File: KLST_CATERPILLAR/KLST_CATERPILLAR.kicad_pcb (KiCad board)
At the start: 6 copper layers, 148.5 x 105 mm, 242 parts, among them J1 Micro_SD_Card_Det_Hirose_DM3AT, J10 HOST(DFP), J11 DAC, J12 ADC, J13 GPIO, J14 ARM_JTAG_SWD(STDC14), J15 TC2070-IDC-NL, J16 MIC_IN, J17 LINE_IN, J18 HEADPHONE_OUT+MIC, J19 LINE_OUT, J2 FPC-40, J3 Battery_18650_Plus, J4 Battery_18650_Minus, J5 UART, J6 UART, J7 MIDI_IN, J8 MIDI_OUT, J9 DEVICE+CHARGE(UFP), Q1 AO3401A, Q2 BCM857BS, Q3 AO3401A, Q4 AO3401A, SW1 BUTTON_RESET, SW2 BUTTON_BOOT_FLASH, SW3 SW_SPDT, SW4 ENCODER, SW5 ENCODER, SW6 BUTTON, SW7 BUTTON, SW8 BUTTON, U1 AMS1117-3.3, U10 MP34DT05TR-A, U11 MP34DT05TR-A, U12 S70KL1282, U13 WM8904CGEFL/V, U14 AMS1117-1.8, U2 STM32H723ZGTx, U3 CAT4139TD-GT3, U4 TP5400, U5 H11L1SR2M, U6 74AHC1G125, U7 ECMF02-2AMX6, U8 TPS2041B, U9 TLV9001IDCK, Y1 16MHz

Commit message: reduced modules
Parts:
- removed C31: 1uF, Capacitor_SMD:C_0805_2012Metric
- removed C32: 4.7uF, Capacitor_SMD:C_0805_2012Metric
- removed C33, C35: 100nF, Capacitor_SMD:C_0805_2012Metric
- removed C34, C36: 22uF, Capacitor_SMD:C_0805_2012Metric
- removed C37: 47uF, Capacitor_SMD:CP_Elec_4x5.4
- removed C38, C39, C40, C41, C42, C43, C44, C45, C52, C53, C54, C55, C56: 100nF, Capacitor_SMD:C_0402_1005Metric
- removed D10, D14, D4: SS14, Diode_SMD:D_SMA
- removed D11: 1N914WT, Diode_SMD:D_SOD-523
- removed D5: LED_STDBY, LED_SMD:LED_0805_2012Metric
- removed D6: LED_CHRG, LED_SMD:LED_0805_2012Metric
- removed D7: SS32, Diode_SMD:D_SMA
- removed H1, H2, H3, H4: M3 Mounting Hole, MountingHole:MountingHole_3.2mm_M3_Pad_Via
- removed J11: DAC, PJ-316A-6A:PJ-316A-6A
- removed J12: ADC, PJ-316A-6A:PJ-316A-6A
- removed J2: FPC-40, THD0525-40CL-GF:CONN-SMD_40P-P0.50-H_THD0525-40CL-GF
- removed J3: Battery_18650_Plus, MY-18650-01:MY-18650-01
- removed J4: Battery_18650_Minus, MY-18650-01:MY-18650-01
- removed J6: UART, Connector_IDC:IDC-Header_2x03_P2.54mm_Horizontal
- removed J7: MIDI_IN, PJ-316A-6A:PJ-316A-6A
- removed J8: MIDI_OUT, PJ-316A-6A:PJ-316A-6A
- removed L2: 22uH, Inductor_SMD:L_Changjiang_FNR4030S
- removed L3: 10uH, Inductor_SMD:L_Changjiang_FNR4030S
- removed Q2: BCM857BS, Package_TO_SOT_SMD:SOT-363_SC-70-6
- removed Q3: AO3401A, Package_TO_SOT_SMD:SOT-23
- removed R18: 20R, Resistor_SMD:R_0805_2012Metric_Pad1.20x1.40mm_HandSolder
- removed R19: 1K, Resistor_SMD:R_1210_3225Metric
- removed R20, R21: 2K, Resistor_SMD:R_0805_2012Metric_Pad1.20x1.40mm_HandSolder
- removed R22: 1.2K, Resistor_SMD:R_0805_2012Metric_Pad1.20x1.40mm_HandSolder
- removed R23: 10K, Resistor_SMD:R_1210_3225Metric
- removed R24: 47K, Resistor_SMD:R_1210_3225Metric
- removed R25, R26, R27, R29, R30, R31, R32, R33, R35, R36, R37, R50, R52, R63: 10K, Resistor_SMD:R_0402_1005Metric
- removed R28, R34, R38, R51, R53: 1K, Resistor_SMD:R_0402_1005Metric
- removed R39: 220R, Resistor_SMD:R_0805_2012Metric
- removed R40, R41: 47R, Resistor_SMD:R_0805_2012Metric
- removed R42: 470R, Resistor_SMD:R_0805_2012Metric
- removed R47: 100K, Resistor_SMD:R_0805_2012Metric
- removed R48, R49: 20K, Resistor_SMD:R_0805_2012Metric
- removed R5, R6: 2.2K, Resistor_SMD:R_0402_1005Metric
- removed R60, R61, R62, R64, R65, R66, R67, R68, R69, R70, R71: 33R, Resistor_SMD:R_0402_1005Metric
- removed SW3: SW_SPDT, MK-12F03-G015:MK-12F03-G015
- removed SW4, SW5: ENCODER, PEC11R-4015F-S0024:PEC11R-4015F-S0024
- removed SW6: BUTTON, Button_Switch_SMD:SW_Push_SPST_NO_Alps_SKRK
- removed SW7, SW8: BUTTON, Cherry_MX:SW_Cherry_MX_PCB
- removed U12: S70KL1282, S70KL1282:BGA24C100P5X5_600X800X100
- removed U3: CAT4139TD-GT3, CAT4139TD-GT3:SOT95P280X100-5N
- removed U4: TP5400, Package_SO:SOP-8_3.9x4.9mm_P1.27mm
- removed U5: H11L1SR2M, Package_DIP:SMDIP-6_W9.53mm
- removed U6: 74AHC1G125, Package_TO_SOT_SMD:SOT-353_SC-70-5
- removed U9: TLV9001IDCK, Package_TO_SOT_SMD:SOT-353_SC-70-5
- J5: footprint Connector_IDC:IDC-Header_2x03_P2.54mm_Horizontal -> Connector_IDC:IDC-Header_2x03_P2.54mm_Vertical_SMD
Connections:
- J13 pad 24: GND -> _BUTTON_PROGRAMMER
- J13 pad 3: GND -> +1.8V
- J5 pad 2: _IDC_SERIAL_01_TX -> _IDC_SERIAL_00_TX
- J5 pad 5: _IDC_SERIAL_01_RX -> _IDC_SERIAL_00_RX
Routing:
- net (no net): track 0.00 -> 562.8 mm, vias 0 -> 13
- net /battery/(BAT_PLUS): track 129.7 -> 0.00 mm, vias 3 -> 0
- net /display/DISPLAY_ANODE_PLUS_22V_OUT: track 67.6 -> 0.00 mm, vias 2 -> 0
- net /display/DISPLAY_CATHODE_MINUS_OUT: track 67.0 -> 0.00 mm, vias 2 -> 0
- net /battery/+5V_OUT: track 38.2 -> 0.00 mm, vias 3 -> 0
- net /MIDI_analog/MIDI_IN_SOURCE(4): track 16.2 -> 0.00 mm
- net /MIDI_analog/MIDI_IN_SINK(5): track 14.7 -> 0.00 mm
- net Net-(U4-PROG): track 14.7 -> 0.00 mm
- net /battery/(LED_CHRG): track 12.6 -> 0.00 mm, vias 1 -> 0
- net /battery/LX: track 10.5 -> 0.00 mm, vias 1 -> 0
- net /MIDI_analog/MIDI_OUT_SOURCE(4): track 10.5 -> 0.00 mm
- net /ADC_DAC/INPUT_SIGNAL: track 8.91 -> 0.00 mm
- net Net-(Q2A-B1): track 8.49 -> 0.00 mm
- net Net-(D11-K): track 8.07 -> 0.00 mm
- net /ADC_DAC/OUTPUT_SIGNAL: track 7.71 -> 0.00 mm
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
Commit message: finished placing components
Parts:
- removed C59: 470pF, Capacitor_SMD:C_0402_1005Metric
- removed C62: 1uF, Capacitor_SMD:C_0402_1005Metric
- removed FB3: 5Ω@100MHz, Inductor_SMD:L_0402_1005Metric
- removed J13: GPIO, Connector_IDC:IDC-Header_2x17_P2.54mm_Horizontal
- removed J16: MIC_IN, PJ-316A-6A:PJ-316A-6A
- removed R76: 2.2K, Resistor_SMD:R_0603_1608Metric
- C1, C2, C29, C3, C30, C4, C47, C48, C5, C7, C88, C89, D1, D2, FB1, FB4, L1, NT1, NT2, Q1, Q4, R12, R13, R14, R15, R16, R17, U1, U10, U11, U14, U8: moved to F.Cu
- moved J19 148.4 mm to (58.0, 59.2), turned to 0 degrees
- moved D1 133.3 mm to (87.5, 151.2), turned to 0 degrees
- moved R1 132.1 mm to (87.5, 149.2), turned to 180 degrees
- moved C88 129.9 mm to (59.6, 150.7)
- moved J17 129.6 mm to (70.0, 59.2), turned to 0 degrees
- moved D9 129.5 mm to (52.7, 102.3)
- moved J5 128.7 mm to (57.2, 90.2), turned to 180 degrees
- moved C60 127.7 mm to (60.7, 77.5), turned to 90 degrees
- moved C57 125.7 mm to (60.7, 80.3), turned to -90 degrees
- moved R80 125.3 mm to (66.0, 69.8), turned to 180 degrees
- moved R73 124.3 mm to (63.0, 76.5), turned to 0 degrees
- moved R77 123.6 mm to (62.7, 78.0), turned to 180 degrees
- moved FB4 122.7 mm to (63.8, 151.0)
- moved R81 122.3 mm to (69.7, 66.8), turned to 90 degrees
- moved R74 122.3 mm to (62.7, 79.8), turned to 180 degrees
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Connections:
- net /audio_codec/(MIC_IN_LEFT) renamed /audio_codec/MIC_IN_MONO
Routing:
- net (no net): track 562.8 -> 0.00 mm, vias 13 -> 0
- net GND: track 331.1 -> 0.00 mm, vias 127 -> 0
- net +5V: track 292.7 -> 0.00 mm, vias 4 -> 0
- net _USB_DEVICE_HOST_VBUS: track 263.9 -> 0.00 mm, vias 6 -> 0
- net _AUDIO_MIC_DATA: track 197.2 -> 0.00 mm, vias 4 -> 0
- net _AUDIO_MIC_CLK: track 192.4 -> 0.00 mm, vias 4 -> 0
- net /USB/VBUS_HOST_OUT: track 152.4 -> 0.00 mm, vias 2 -> 0
- net +3.3V: track 130.1 -> 0.00 mm, vias 58 -> 0
- net _LED_01: track 120.1 -> 0.00 mm, vias 5 -> 0
- net _MECH_BUTTON_01: track 106.8 -> 0.00 mm, vias 4 -> 0
- net _ENCODER_01_BUTTON: track 105.9 -> 0.00 mm, vias 4 -> 0
- net _AUDIO_CODEC_I2C_SCL: track 98.0 -> 0.00 mm, vias 3 -> 0
- net _AUDIO_CODEC_I2C_SDA: track 96.7 -> 0.00 mm, vias 3 -> 0
- net _ENCODER_00_B: track 90.4 -> 0.00 mm, vias 2 -> 0
- net _LED_00: track 83.8 -> 0.00 mm, vias 1 -> 0
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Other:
- board size 148.5 x 105 mm -> 40 x 125 mm
- board text removed: "+"
- board text removed: "-"
- board text removed: "..... ..... ..ADC"
- board text removed: "..... ..... ..DAC"
- board text removed: "..... ....M IC_IN"
- board text removed: "..... ...MI DI_IN"
- board text removed: "..... ..MID I_OUT"
- board text removed: "PRG"

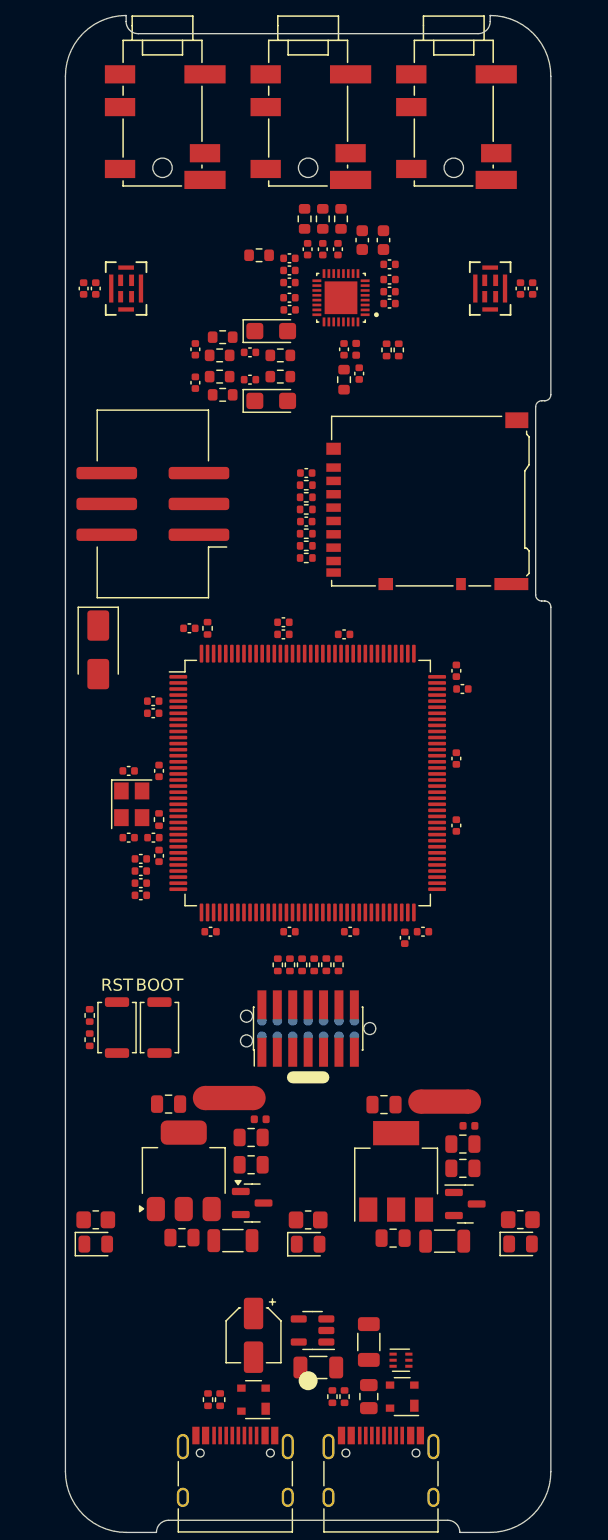
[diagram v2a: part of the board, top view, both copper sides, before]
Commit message: routed modules ( not finished )
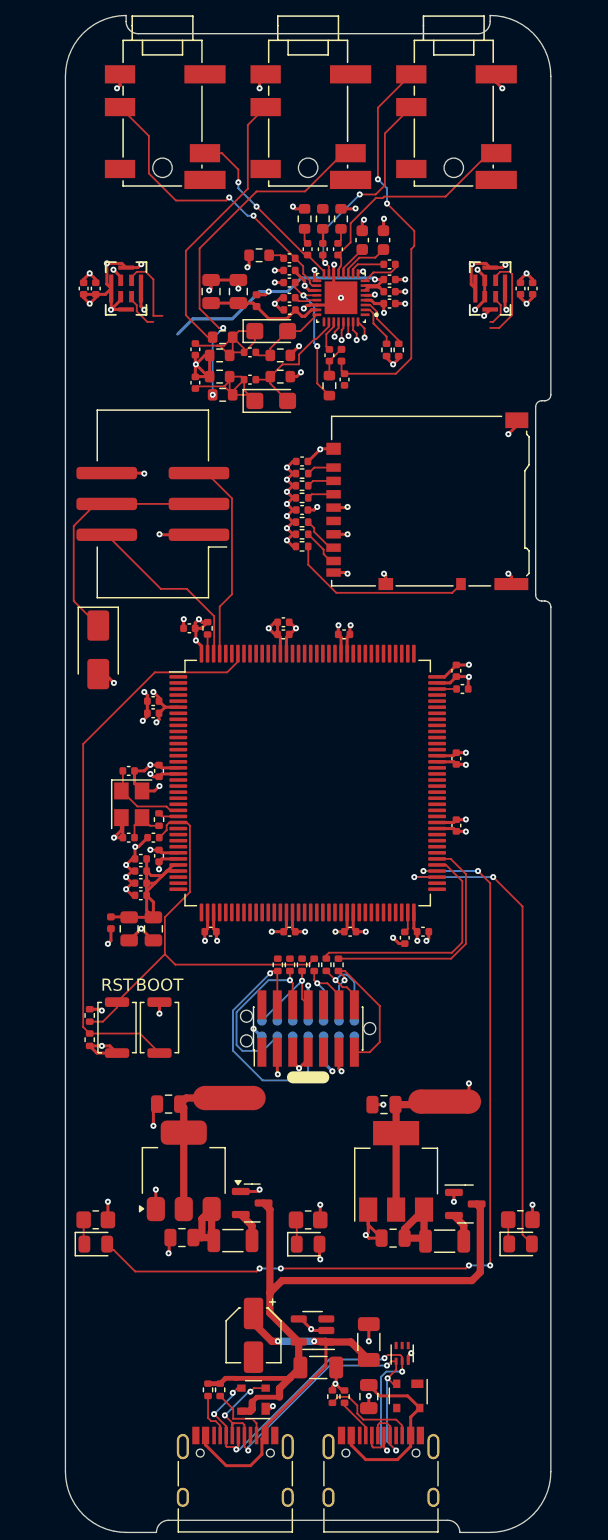
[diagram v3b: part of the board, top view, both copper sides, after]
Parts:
- moved C71 72.0 mm to (62.0, 72.8), turned to 90 degrees
- moved C69 69.7 mm to (64.2, 72.8), turned to 90 degrees
- moved L4 67.5 mm to (65.8, 73.5), turned to -90 degrees
- moved L1 33.9 mm to (53.8, 124.8), turned to 90 degrees
- moved C3 32.7 mm to (55.2, 125.3), turned to -90 degrees
- moved C4 32.2 mm to (57.2, 125.3), turned to -90 degrees
- moved C58 1.30 mm to (73.0, 80.0)
- moved C61 1.30 mm to (71.8, 78.0)
- moved FB2 1.30 mm to (72.8, 78.0)
- moved R75 1.30 mm to (71.8, 80.5)
- moved C29 1.01 mm to (69.5, 90.8)
- moved C30 1.01 mm to (69.5, 86.8)
- moved R12 1.01 mm to (69.5, 93.8)
- moved R13 1.01 mm to (69.5, 92.8)
- moved R14 1.01 mm to (69.5, 91.8)
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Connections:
- U13 pad 25: /audio_codec/MIC_IN_RIGHT -> unconnected-(U13-IN1R/DMICDAT2-Pad25)
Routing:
- net GND: track 0.00 -> 175.4 mm, vias 0 -> 87
- net +3.3V: track 0.00 -> 80.9 mm, vias 0 -> 39
- net _LED_01: track 0.00 -> 71.2 mm, vias 0 -> 6
- net +5V: track 0.00 -> 52.7 mm
- net BOOT0: track 0.00 -> 46.9 mm
- net /USB/USB_CONNECTOR_MINUS: track 0.00 -> 39.9 mm, vias 0 -> 6
- net _LED_00: track 0.00 -> 39.9 mm, vias 0 -> 2
- net /USB/USB_CONNECTOR_PLUS: track 0.00 -> 39.0 mm, vias 0 -> 6
- net NRST: track 0.00 -> 36.5 mm
- net /audio_codec/MIC_IN_MONO: track 0.00 -> 33.4 mm, vias 0 -> 2
- net /USB/VBUS_HOST_OUT: track 0.00 -> 29.5 mm, vias 0 -> 2
- net /audio_codec/(LINE_IN_LEFT): track 0.00 -> 29.1 mm, vias 0 -> 2
- net /audio_codec/LINE_OUT_RIGHT: track 0.00 -> 24.9 mm, vias 0 -> 2
- net +1.8V: track 0.00 -> 23.6 mm, vias 0 -> 2
- net /audio_codec/(LINE_IN_RIGHT): track 0.00 -> 22.8 mm
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
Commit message: finished routing
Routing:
- net _AUDIO_MIC_DATA: track 13.8 -> 89.6 mm, vias 0 -> 2
- net _AUDIO_MIC_CLK: track 5.86 -> 81.1 mm, vias 0 -> 3
- net +1.8V: track 23.6 -> 98.6 mm, vias 2 -> 3
- net _USB_DEVICE_HOST_VBUS: track 15.4 -> 80.1 mm, vias 0 -> 2
- net _USB_DEVICE_HOST_P: track 0.00 -> 63.7 mm, vias 0 -> 2
- net _USB_DEVICE_HOST_N: track 0.00 -> 62.5 mm, vias 0 -> 2
- net _AUDIO_CODEC_I2C_SDA: track 4.58 -> 60.1 mm, vias 0 -> 2
- net _AUDIO_CODEC_I2C_SCL: track 3.75 -> 59.2 mm, vias 0 -> 2
- net _AUDIO_CODEC_SAI_SD_IN: track 1.62 -> 54.5 mm, vias 1 -> 2
- net _AUDIO_CODEC_SAI_FS: track 1.17 -> 46.4 mm, vias 1 -> 2
- net _AUDIO_CODEC_SAI_SCK: track 1.56 -> 45.7 mm, vias 1 -> 2
- net _AUDIO_CODEC_SAI_MCLK: track 1.35 -> 44.9 mm, vias 1 -> 2
- net _AUDIO_CODEC_SAI_SD_OUT: track 1.52 -> 39.2 mm, vias 1 -> 2
- net _SWD_CLK: track 0.00 -> 29.7 mm, vias 0 -> 2
- net _SWD_OUT: track 0.00 -> 28.8 mm, vias 0 -> 2
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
